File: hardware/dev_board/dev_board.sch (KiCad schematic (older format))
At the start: 3 parts

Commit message: finished schematic
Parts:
- added C? (x2): C_4u7, personal:C_0805, symbol personal:C_4u7
- added C? (x13): C_0u1, personal:C_0805, symbol personal:C_0u1
- added C?: C_220u, personal:UWT0G221MCL6GS, symbol personal:C_220u
- added C? (x2): C_8p, personal:C_0805, symbol personal:C_8p
- added C?: C_1u, personal:C_0805, symbol personal:C_1u
- added C? (x2): C_10u, personal:C_0805, symbol personal:C_10u
- added C?: C_22u, personal:C_0805, symbol personal:C_22u
- added D? (x2): D_Schottky_10V_3A, Diodes_SMD:D_SOD-323F, symbol personal:D_Schottky_10V_3A
- added D?: D_Schottky_x2_20V, personal:SOT1061, symbol personal:D_Schottky_x2_20V
- added D? (x4): LED_0805_Green, personal:LED_0805, symbol personal:LED_0805_Green
- added F? (x2): PTC_6V_1A, Resistors_SMD:R_0805_HandSoldering, symbol personal:PTC_6V_1A
- added J?: Micro_USB, Connectors_USB:USB_Micro-B_Molex_47346-0001, symbol personal:Micro_USB
- added J?: Conn_02x03, personal:TSW-103-07-F-D, symbol personal:Conn_02x03
- added J?: 105162-0001, personal:105162-0001, symbol personal:105162-0001
- added J? (x3): Conn_01x02, personal:header_01x02, symbol personal:Conn_01x02
- added J?: Conn_01x10, personal:header_01x10, symbol personal:Conn_01x10
- added J? (x3): Conn_01x04, personal:header_01x04, symbol personal:Conn_01x04
- added J?: Conn_01x06, personal:header_01x06, symbol personal:Conn_01x06
- added J?: Conn_01x11, personal:header_01x11, symbol personal:Conn_01x11
- added R?: R_1K, personal:R_0805, symbol personal:R_1K
- added R?: R_10K, personal:R_0805, symbol personal:R_10K
- added R? (x2): R_22, personal:R_0805, symbol personal:R_22
- added R?: R_120, personal:R_0805, symbol personal:R_120
- added R?: R_2K18, personal:R_0805, symbol personal:R_2K18
- added R? (x3): R_51.1, personal:R_0805, symbol personal:R_51.1
- added R? (x6): R_100K, personal:R_0805, symbol personal:R_100K
- added U?: MCP131T-300E_TT, personal:SOT-23, symbol personal:MCP131T-300E_TT
- added U?: LDO_600MA, personal:SOT-25_DIO, symbol personal:LDO_600MA
- added U?: OKL-T_1-W12P-C, personal:OKL-T1-W12P-C, symbol personal:OKL-T_1-W12P-C
- added U?: Barometer_MS5607, personal:MS561101BA03-50, symbol personal:Barometer_MS5607
- added U?: FRAM_4K, Housings_SOIC:SOIC-8_3.9x4.9mm_Pitch1.27mm, symbol personal:FRAM_4K
- added Y?: Crystal_24MHZ, personal:NX3225SA-24.000M-STD-CSR-1, symbol personal:Crystal_24MHZ
- U?: footprint drone_footprints:BMI088 -> personal:BMI088
- U?: footprint drone_footprints:LIS3MDLTR -> personal:LIS3MDLTR
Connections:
- net at U?.1 (VBAT): now also C?.1, D?.1 (K)
- net SPI2_MISO: now reaches U?.10 (PC2)
- net SPI2_MISO: now also J?.2, U?.5 (SI)
- net SPI2_MOSI: now reaches U?.11 (PC3)
- net SPI2_MOSI: now also J?.3, U?.2 (SO)
- net GND: now reaches U?.12 (VSSA)
- net GND: now also U?.12 (RES), U?.18 (VSS), U?.2 (NC), U?.2 (RES), U?.3 (GND), U?.31 (VSS), U?.4 (GNDA), U?.47 (VSS), U?.6 (GNDio), U?.63 (VSS), U?.7 (PS), C?.1, C?.1, C?.1, C?.1, C?.1, C?.1, C?.1, C?.2, C?.2, C?.2, C?.2, C?.2, C?.2, C?.2, C?.2, C?.2, C?.2, C?.2, C?.2, C?.2, C?.2, C?.2, J?.10 (GND_1), J?.11 (GND_2), J?.12 (GND_3), J?.13 (GND_4), J?.2, J?.2, J?.2, J?.4, J?.4, J?.5 (GND), J?.6, J?.6 (Pin_6), J?.6 (VSS), R?.2, R?.2, R?.2, R?.2, R?.2, R?.2, U?.11 (GND), U?.2 (GND), U?.2 (PS), U?.3 (GND), U?.3 (GND), U?.3 (VSS), U?.4 (Vss), U?.7 (GND), Y?.2, Y?.4
- net 3V3: now reaches U?.13 (VREF+)
- net 3V3: now also U?.11 (VDDIO), U?.19 (VDD), U?.3 (VDD), U?.32 (VDD), U?.48 (VDD), U?.5 (VDD), U?.6 (VDD_IO), U?.64 (VDD), C?.1, C?.1, C?.1, C?.1, C?.1, C?.1, C?.1, C?.1, C?.1, C?.1, C?.1, C?.1, C?.2, D?.2 (A), J?.1, J?.1, J?.1, J?.1 (Pin_1), J?.4 (VDD), R?.1, R?.1, R?.1, R?.1, R?.1, R?.1, R?.2, U?.2 (VDD), U?.3 (EN), U?.3 (~WP), U?.5 (VO), U?.7 (~HOLD), U?.8 (Vdd)
- net ADC_IN0: now reaches U?.14 (PA0)
- net ADC_IN0: now also J?.1
- net ADC_IN1: now reaches U?.15 (PA1)
- net ADC_IN1: now also J?.2
- net USART2_TX: now reaches U?.16 (PA2)
- net USART2_TX: now also J?.2
- net USART2_RX: now reaches U?.17 (PA3)
- net USART2_RX: now also J?.3
- net SD_DETECT: now reaches U?.2 (PC13)
- net SD_DETECT: now also J?.9 (DET), R?.2
- net PA4: now reaches U?.20 (PA4)
- net PA4: now also J?.3
- net SPI1_SCK: now reaches U?.21 (PA5)
- net SPI1_SCK: now also U?.1 (SCL/SPC), U?.8 (SCx), J?.1, U?.8 (SCLK)
- net SPI1_MISO: now reaches U?.22 (PA6)
- net SPI1_MISO: now also U?.10 (SD02), U?.15 (SD01), U?.9 (SDO/SA1), J?.2, U?.6 (SDO)
- net SPI1_MOSI: now reaches U?.23 (PA7)
- net SPI1_MOSI: now also U?.11 (SDA/SDI/SDO), U?.9 (SDx), J?.3, U?.7 (SDI/A)
- net ACCEL_CS: now reaches U?.24 (PC4)
- net ACCEL_CS: now also U?.14 (CSB1), J?.6
- net GYRO_CS: now reaches U?.25 (PC5)
- net GYRO_CS: now also U?.5 (CSB2), J?.7
- net BARO_CS: now reaches U?.26 (PB0)
- net BARO_CS: now also J?.10, U?.4 (CSB), U?.5 (CSB)
- net ~FRAM_CS: now reaches U?.27 (PB1)
- net ~FRAM_CS: now also J?.4, U?.1 (~CS)
- net SPI3_AUX_CS: now reaches U?.28 (PB2)
- net SPI3_AUX_CS: now also J?.5
- net SPI2_SCK: now reaches U?.29 (PB10)
- net SPI2_SCK: now also J?.1, U?.6 (SCK)
- net at U?.3 (PC14): now also D?.2 (A)
- net at U?.30 (VCAP1): now also C?.1
- net PB12: now reaches U?.33 (PB12)
- net PB12: now also J?.8
- net PB13: now reaches U?.34 (PB13)
- net PB13: now also J?.9
- net PB14: now reaches U?.35 (PB14)
- net PB14: now also J?.10
- net PB15: now reaches U?.36 (PB15)
- net PB15: now also J?.11
- net ACCEL_DRDY: now reaches U?.37 (PC6)
- net ACCEL_DRDY: now also U?.16 (INT1), J?.8
- net GYRO_DRDY: now reaches U?.38 (PC7)
- net GYRO_DRDY: now also U?.12 (INT3), J?.9
- net SDIO_D0: now reaches U?.39 (PC8)
- net SDIO_D0: now also J?.7 (DAT0), R?.2
- net at U?.4 (PC15): now also D?.2 (A)
- net SDIO_D1: now reaches U?.40 (PC9)
- net PA8: now reaches U?.41 (PA8)
- net PA8: now also J?.4
- net USART1_TX: now reaches U?.42 (PA9)
- net USART1_TX: now also J?.2 (Pin_2)
- net PA10: now reaches U?.43 (PA10)
- net PA10: now also J?.5
- net OTG_FS_D_N: now reaches U?.44 (PA11)
- net OTG_FS_D_N: now also R?.2
- net OTG_FS_D_P: now reaches U?.45 (PA12)
- net OTG_FS_D_P: now also R?.2
- net SWDIO: now reaches U?.46 (PA13)
- net SWDIO: now also J?.4 (Pin_4)
- net SWCLK: now reaches U?.49 (PA14)
- net SWCLK: now also J?.5 (Pin_5)
- net at U?.5 (PH0): now also C?.1, Y?.3
- net PA15: now reaches U?.50 (PA15)
- net PA15: now also J?.6
- net SDIO_D2: now reaches U?.51 (PC10)
- net SDIO_D2: now also J?.1 (DAT2), R?.2
- net SDIO_D3: now reaches U?.52 (PC11)
- net SDIO_D3: now also J?.2 (CD/DAT3), R?.2
- net SDIO_CK: now reaches U?.53 (PC12)
- net SDIO_CK: now also J?.5 (CLK)
- net SDIO_CMD: now reaches U?.54 (PD2)
- net SDIO_CMD: now also J?.3 (CMD), R?.2
- net SPI3_SCK: now reaches U?.55 (PB3)
- net SPI3_SCK: now also J?.2
- net SPI3_MISO: now reaches U?.56 (PB4)
- net SPI3_MISO: now also J?.3
- net SPI3_MOSI: now reaches U?.57 (PB5)
- net SPI3_MOSI: now also J?.4
- net I2C1_SCL: now reaches U?.58 (PB6)
- net I2C1_SCL: now also J?.2
- net USART1_RX: now reaches U?.59 (PB7)
- net USART1_RX: now also J?.3 (Pin_3)
- net at U?.6 (PH1): now also C?.2, Y?.1
- net at U?.60 (BOOT0): now also R?.1
- net PB8: now reaches U?.61 (PB8)
- net PB8: now also J?.7
- net I2C1_SDA: now reaches U?.62 (PB9)
- net I2C1_SDA: now also J?.3
- net at U?.7 (NRST): now also U?.1 (~RST)
- net MAG_CS: now reaches U?.8 (PC0)
- net MAG_CS: now also U?.10 (CS), J?.4
- net MAG_DRDY: now reaches U?.9 (PC1)
- net MAG_DRDY: now also U?.8 (DRDY), J?.5
- net at U?.4 (C1): now also C?.2
- new net: D?.2 (A), R?.1
- new net: J?.2 (D-), R?.1
- new net: J?.3 (D+), R?.1
- new net: D?.3 (K), F?.1
- new net: D?.1 (K), R?.1 (x4)
- new net: C?.2, D?.1 (K), F?.2, U?.1 (VI)
- new net: C?.2, J?.1, U?.2 (VIN)
- new net: R?.1, U?.6 (TRIM)
- new net: C?.2, U?.1 (VDD)
- new net: J?.8 (DAT1), R?.2
- new net: F?.1, J?.1
- new net 5V: D?.2 (A), D?.2 (A), F?.2, J?.1
- new net BUCK_5V: D?.1 (A), U?.4 (VOUT)
- new net USB_5V: C?.2, D?.2 (A), J?.1 (VBUS)
- no-connect marks 0 -> 5
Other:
- note added: "5V Output"
- note added: "5V Power Circuits"
- note added: "Barometer"
- note added: "Buck Converter Power\n5 < Vin <= 14"
- note added: "Debug & Programming"
- note added: "Extra Pins\n"
- note added: "I2C1 Output"
- note added: "IMU"
- note added: "LDO Power\n3.3 <= Vin < 5"
- note added: "Magnetometer"
- note added: "MicroSD"
- note added: "Non-Volatile Memory"
- note added: "Power Watchdog"
- note added: "Real Time Clock"
- note added: "SPI1 Pinout"
- note added: "SPI2 Pinout"
- note added: "SPI3 Output"
- note added: "UART2 Output"
- note added: "USB Micro"
- moved on the sheet: U?

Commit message: Fixed a few errors
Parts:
- added D8: TVS_DIODE_14V, Capacitors_SMD:C_0402, symbol personal:TVS_DIODE_14V
- added R16, R17: R_10K, personal:R_0805, symbol personal:R_10K
- gave numbers to parts that had none: 67
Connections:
- net 3V3: now also R16.1, R17.1
- net 5V: now also D8.2 (A2)
- net GND: now also D8.1 (A1)
- net I2C1_SCL: now also R16.2
- net I2C1_SDA: now also R17.2
- net SDIO_D1: now also J12.8 (DAT1), R10.2
- no-connect marks 5 -> 7
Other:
- moved on the sheet: D4, J11, J9, R5

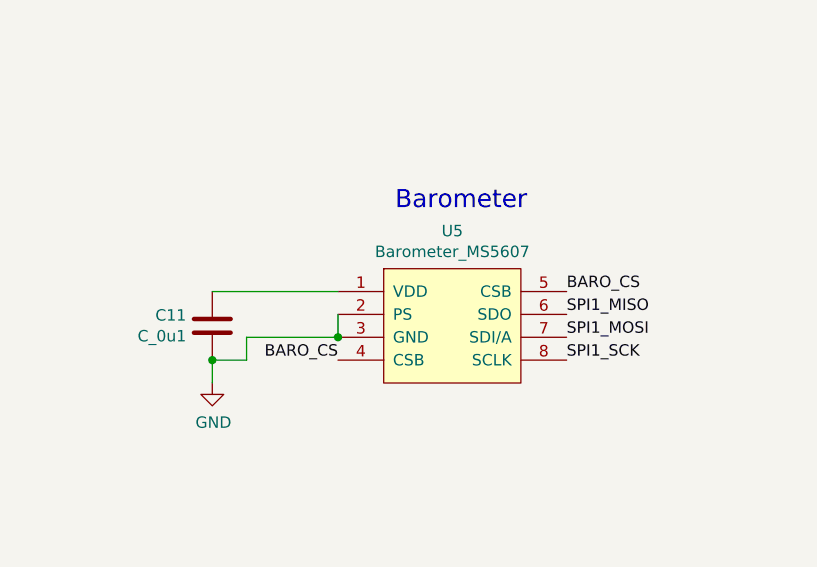
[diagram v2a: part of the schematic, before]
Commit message: fixed power issue with schematic
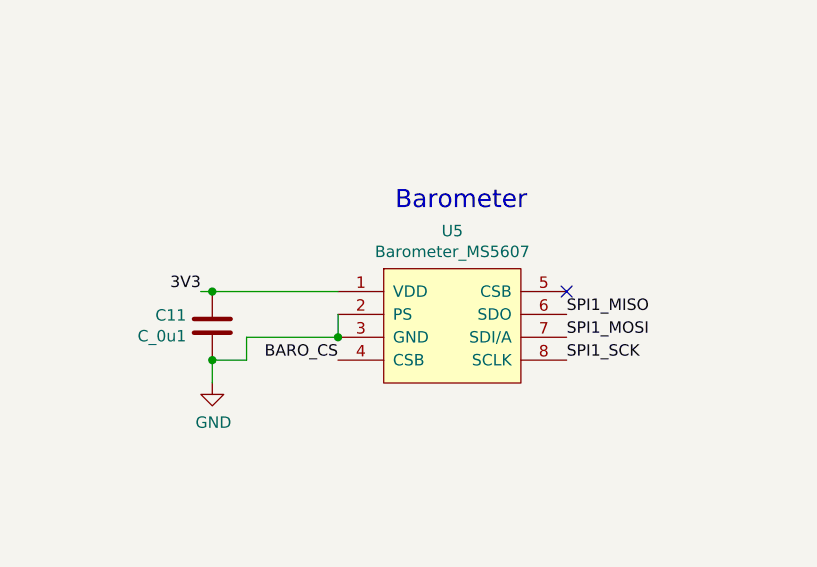
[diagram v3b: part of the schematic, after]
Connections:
- net 3V3: now also C11.2, U5.1 (VDD)
- net BARO_CS: no longer U5.5 (CSB)
- no-connect marks 7 -> 8
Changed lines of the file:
@@
 Text Label 9450 9800 2    50   ~ 0
-BARO_CS
-Text Label 10450 9500 0    50   ~ 0
 BARO_CS
 Text Label 11650 4250 2    50   ~ 0
@@
 NoConn ~ 7500 9600
 NoConn ~ 7500 9800
+Wire Wire Line
+	8900 9500 8850 9500
+Connection ~ 8900 9500
+Text Label 8850 9500 2    50   ~ 0
+3V3
+NoConn ~ 10450 9500
 $EndSCHEMATC

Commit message: added the all important axis guide and started layout
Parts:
- U7: footprint Package_QFP:LQFP-64_10x10mm_P0.5mm -> personal:STM32F401RCT6
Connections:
- net ACCEL_DRDY: now also U7.35 (PB14); no longer U7.37 (PC6)
- net BARO_CS: now also U7.33 (PB12); no longer U7.26 (PB0)
- net GYRO_DRDY: now also U7.36 (PB15); no longer U7.38 (PC7)
- net ~FRAM_CS: now also U7.34 (PB13); no longer U7.27 (PB1)
- net PB12 renamed TIM3_CH1
- net TIM3_CH1: now also U7.37 (PC6); no longer U7.33 (PB12)
- net PB13 renamed TIM3_CH2
- net TIM3_CH2: now also U7.38 (PC7); no longer U7.34 (PB13)
- net PB14 renamed TIM3_CH3
- net TIM3_CH3: now also U7.26 (PB0); no longer U7.35 (PB14)
- net PB15 renamed TIM3_CH4
- net TIM3_CH4: now also U7.27 (PB1); no longer U7.36 (PB15)
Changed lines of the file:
@@
 F 0 "U7" H 12300 5631 50  0000 C CNN
 F 1 "STM32F401RCTx" H 12300 5540 50  0000 C CNN
-F 2 "Package_QFP:LQFP-64_10x10mm_P0.5mm" H 11750 2050 50  0001 R CNN
+F 2 "personal:STM32F401RCT6" H 11750 2050 50  0001 R CNN
 F 3 "http://www.st.com/st-web-ui/static/active/en/resource/technical/document/datasheet/DM00086815.pdf" H 12350 3750 50  0001 C CNN
 	1    12350 3750
@@
 Text Label 11650 4350 2    50   ~ 0
 GYRO_CS
-Text Label 11650 4450 2    50   ~ 0
+Text Label 12950 5250 0    50   ~ 0
 ACCEL_DRDY
-Text Label 11650 4550 2    50   ~ 0
+Text Label 12950 5350 0    50   ~ 0
 GYRO_DRDY
-Text Label 12950 3950 0    50   ~ 0
+Text Label 12950 5050 0    50   ~ 0
 BARO_CS
 Text Label 11650 3850 2    50   ~ 0
@@
 Text Label 12100 7300 2    50   ~ 0
 ~FRAM_CS
-Text Label 12950 4050 0    50   ~ 0
+Text Label 12950 5150 0    50   ~ 0
 ~FRAM_CS
 $Comp
@@
 Text Label 4150 8100 0    50   ~ 0
 PB8
-Text Label 12950 5050 0    50   ~ 0
-PB12
-Text Label 12950 5150 0    50   ~ 0
-PB13
-Text Label 12950 5250 0    50   ~ 0
-PB14
-Text Label 12950 5350 0    50   ~ 0
-PB15
-Text Label 4150 8200 0    50   ~ 0
-PB12
-Text Label 4150 8300 0    50   ~ 0
-PB13
-Text Label 4150 8400 0    50   ~ 0
-PB14
-Text Label 4150 8500 0    50   ~ 0
-PB15
 Text Notes 10200 1850 0    79   ~ 0
 Power Watchdog
@@
 3V3
 NoConn ~ 10450 9500
+Text Label 12950 3950 0    50   ~ 0
+TIM3_CH3
+Text Label 12950 4050 0    50   ~ 0
+TIM3_CH4
+Text Label 4150 8400 0    50   ~ 0
+TIM3_CH3
+Text Label 4150 8500 0    50   ~ 0
+TIM3_CH4
+Text Label 11650 4450 2    50   ~ 0
+TIM3_CH1
+Text Label 11650 4550 2    50   ~ 0
+TIM3_CH2
+Text Label 4150 8200 0    50   ~ 0
+TIM3_CH1
+Text Label 4150 8300 0    50   ~ 0
+TIM3_CH2
 $EndSCHEMATC

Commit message: finished layout
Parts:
- removed U7: STM32F401RCTx, personal:STM32F401RCT6, symbol MCU_ST_STM32F4:STM32F401RCTx
- added U7: STM32F401RCTx, personal:LQFP-64_10x10mm_Pitch0.5mm, symbol personal:STM32F401RCTx
- D1, D7: footprint Diodes_SMD:D_SOD-323F -> personal:D_SOD-323F
- D8: footprint Capacitors_SMD:C_0402 -> personal:C_0402
- F1, F2: footprint Resistors_SMD:R_0805_HandSoldering -> personal:R_0805_HandSoldering
- J1: footprint Connectors_USB:USB_Micro-B_Molex_47346-0001 -> personal:USB_Micro-B_Molex_47346-0001
- U8: footprint Housings_SOIC:SOIC-8_3.9x4.9mm_Pitch1.27mm -> personal:SOIC-8_3.9x4.9mm_Pitch1.27mm
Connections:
- net PB8 is gone; now on net TIM3_CH4: J10.7
- net 3V3: now also U7.13 (VREF+), U7.19 (VDD), U7.32 (VDD), U7.48 (VDD), U7.64 (VDD)
- net ACCEL_CS: now also J5.7, U7.24 (PC4); no longer J5.6
- net ACCEL_DRDY: now also U7.35 (PB14)
- net BARO_CS: now also J5.4, U7.33 (PB12); no longer J5.10
- net GND: now also U7.12 (VSSA), U7.18 (VSS), U7.31 (VSS), U7.47 (VSS), U7.63 (VSS)
- net GYRO_CS: now also J5.6, U7.25 (PC5); no longer J5.7
- net GYRO_DRDY: now also J5.5, U7.36 (PB15); no longer J5.9
- net I2C1_SCL: now also U7.58 (PB6)
- net I2C1_SDA: now also U7.62 (PB9)
- net MAG_CS: now also J5.9, U7.15 (PA1); no longer J5.4
- net MAG_DRDY: now also J5.10, U7.14 (PA0); no longer J5.5
- net OTG_FS_D_N: now also U7.44 (PA11)
- net OTG_FS_D_P: now also U7.45 (PA12)
- net PA10: now also J10.9, U7.43 (PA10); no longer J10.5
- net PA15: now also J10.10, U7.50 (PA15); no longer J10.6
- net PA8: now also J10.8, U7.41 (PA8); no longer J10.4
- net SDIO_CK: now also U7.53 (PC12)
- net SDIO_CMD: now also U7.54 (PD2)
- net SDIO_D0: now also U7.39 (PC8)
- net SDIO_D1: now also U7.40 (PC9)
- net SDIO_D2: now also U7.51 (PC10)
- net SDIO_D3: now also U7.52 (PC11)
- net SD_DETECT: now also U7.2 (PC13)
- net SPI1_MISO: now also U7.22 (PA6)
- net SPI1_MOSI: now also U7.23 (PA7)
- net SPI1_SCK: now also U7.21 (PA5)
- net SPI2_MISO: now also U7.10 (PC2)
- net SPI2_MOSI: now also U7.11 (PC3)
- net SPI2_SCK: now also U7.29 (PB10)
- net SPI3_AUX_CS: now also U7.61 (PB8)
- net SPI3_MISO: now also U7.56 (PB4)
- net SPI3_MOSI: now also U7.57 (PB5)
- net SPI3_SCK: now also U7.55 (PB3)
- net SWCLK: now also U7.49 (PA14)
- net SWDIO: now also U7.46 (PA13)
- net TIM3_CH1: now also J10.4, U7.37 (PC6); no longer J10.8
- net TIM3_CH2: now also J10.5, U7.38 (PC7); no longer J10.9
- net TIM3_CH3: now also J10.6, U7.26 (PB0); no longer J10.10
- net TIM3_CH4: now also U7.27 (PB1); no longer J10.11
- net USART1_RX: now also U7.59 (PB7)
- net USART1_TX: now also U7.42 (PA9)
- net USART2_RX: now also U7.17 (PA3)
- net USART2_TX: now also U7.16 (PA2)
- net ~FRAM_CS: now also U7.20 (PA4)
- net at C16.1, D7.1 (K): now also U7.1 (VBAT)
- net at D5.2 (A): now also U7.3 (PC14)
- net at C15.1: now also U7.30 (VCAP1)
- net at D6.2 (A): now also U7.4 (PC15)
- net at C13.1, Y1.3: now also U7.5 (PH0)
- net at C14.2, Y1.1: now also U7.6 (PH1)
- net at R15.1: now also U7.60 (BOOT0)
- net at U6.1 (~RST): now also U7.7 (NRST)
- net ADC_IN0 renamed ADC_IN11
- net ADC_IN11: now also U7.9 (PC1)
- net ADC_IN1 renamed ADC_IN10
- net ADC_IN10: now also U7.8 (PC0)
- net PA4 renamed PB13
- net PB13: now also U7.34 (PB13)
- new net PB2: J10.11, U7.28 (PB2)
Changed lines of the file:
@@
 $EndDescr
-$Comp
-L MCU_ST_STM32F4:STM32F401RCTx U7
-U 1 1 60302E32
-P 12350 3750
-F 0 "U7" H 12300 5631 50  0000 C CNN
-F 1 "STM32F401RCTx" H 12300 5540 50  0000 C CNN
-F 2 "personal:STM32F401RCT6" H 11750 2050 50  0001 R CNN
-F 3 "http://www.st.com/st-web-ui/static/active/en/resource/technical/document/datasheet/DM00086815.pdf" H 12350 3750 50  0001 C CNN
-	1    12350 3750
-	1    0    0    -1
-$EndComp
 $Comp
 L personal:BMI088 U4
@@
 Wire Wire Line
 	12550 1550 12800 1550
-Wire Wire Line
-	12250 2050 12350 2050
-Connection ~ 12550 2050
-Connection ~ 12350 2050
-Wire Wire Line
-	12350 2050 12450 2050
-Connection ~ 12450 2050
-Wire Wire Line
-	12450 2050 12550 2050
 Wire Wire Line
 	14600 1550 14150 1550
@@
 Wire Wire Line
 	11200 3700 11200 3450
-Wire Wire Line
-	12150 5550 12250 5550
-Connection ~ 12250 5550
-Wire Wire Line
-	12250 5550 12350 5550
-Connection ~ 12350 5550
-Wire Wire Line
-	12350 5550 12450 5550
-Connection ~ 12450 5550
-Wire Wire Line
-	12450 5550 12550 5550
 $Comp
 L power:GND #PWR031
@@
 Wire Wire Line
 	12550 5600 12550 5550
-Connection ~ 12550 5550
 $Comp
 L personal:MCP131T-300E_TT U6
@@
 F 0 "J1" H 1107 1867 50  0000 C CNN
 F 1 "Micro_USB" H 1107 1776 50  0000 C CNN
-F 2 "Connectors_USB:USB_Micro-B_Molex_47346-0001" H 1650 1000 50  0001 C CNN
+F 2 "personal:USB_Micro-B_Molex_47346-0001" H 1650 1000 50  0001 C CNN
 F 3 "https://www.digikey.com/products/en?keywords=WM17141CT-ND" H 1200 1350 50  0001 C CNN
 F 4 "WM17141CT-ND" H 1600 1100 50  0001 C CNN "DPN"
@@
 F 0 "F2" H 4850 2125 50  0000 C CNN
 F 1 "PTC_6V_1A" H 4850 2034 50  0000 C CNN
-F 2 "Resistors_SMD:R_0805_HandSoldering" H 4950 2350 50  0001 L CNN
+F 2 "personal:R_0805_HandSoldering" H 4950 2350 50  0001 L CNN
 F 3 "" V 4850 1900 50  0001 C CNN
 F 4 "507-1813-1-ND" H 5250 2150 50  0001 C CNN "DPN"
@@
 F 0 "U8" H 12450 7493 50  0000 C CNN
 F 1 "FRAM_4K" H 12400 6850 50  0001 C CNN
-F 2 "Housings_SOIC:SOIC-8_3.9x4.9mm_Pitch1.27mm" H 12350 7600 50  0001 C CNN
+F 2 "personal:SOIC-8_3.9x4.9mm_Pitch1.27mm" H 12350 7600 50  0001 C CNN
 F 3 "https://www.cypress.com/file/136461/download" H 11900 7950 50  0001 C CNN
 F 4 "428-3209-ND" H 11600 7600 50  0001 C CNN "DPN"
@@
 	1    0    0    -1
 $EndComp
-Text Label 12950 2250 0    50   ~ 0
-ADC_IN0
-Text Label 12950 2350 0    50   ~ 0
-ADC_IN1
+Text Label 11650 3950 2    50   ~ 0
+ADC_IN11
+Text Label 11650 3850 2    50   ~ 0
+ADC_IN10
 Text Label 12950 2450 0    50   ~ 0
 USART2_TX
@@
 Text Label 12950 5050 0    50   ~ 0
 BARO_CS
-Text Label 11650 3850 2    50   ~ 0
+Text Label 12950 2350 0    50   ~ 0
 MAG_CS
-Text Label 11650 3950 2    50   ~ 0
+Text Label 12950 2250 0    50   ~ 0
 MAG_DRDY
 Text Label 4250 9700 0    50   ~ 0
@@
 Text Label 12100 7300 2    50   ~ 0
 ~FRAM_CS
-Text Label 12950 5150 0    50   ~ 0
+Text Label 12950 2650 0    50   ~ 0
 ~FRAM_CS
 $Comp
@@
 F 0 "F1" H 1800 4175 50  0000 C CNN
 F 1 "PTC_6V_1A" H 1800 4084 50  0000 C CNN
-F 2 "Resistors_SMD:R_0805_HandSoldering" H 1900 4400 50  0001 L CNN
+F 2 "personal:R_0805_HandSoldering" H 1900 4400 50  0001 L CNN
 F 3 "" V 1800 3950 50  0001 C CNN
 F 4 "507-1813-1-ND" H 2200 4200 50  0001 C CNN "DPN"
@@
 F 0 "D7" H 11750 1350 50  0000 C CNN
 F 1 "D_Schottky_10V_3A" H 11600 1450 50  0000 C CNN
-F 2 "Diodes_SMD:D_SOD-323F" H 12250 1850 50  0001 C CNN
+F 2 "personal:D_SOD-323F" H 12250 1850 50  0001 C CNN
 F 3 "~" H 11750 1550 50  0001 C CNN
 F 4 "1727-3852-1-ND" H 12150 1750 50  0001 C CNN "DPN"
@@
 F 0 "D1" H 2850 3600 50  0000 C CNN
 F 1 "D_Schottky_10V_3A" H 2700 3700 50  0000 C CNN
-F 2 "Diodes_SMD:D_SOD-323F" H 3350 4100 50  0001 C CNN
+F 2 "personal:D_SOD-323F" H 3350 4100 50  0001 C CNN
 F 3 "~" H 2850 3800 50  0001 C CNN
 F 4 "1727-3852-1-ND" H 3250 4000 50  0001 C CNN "DPN"
@@
 	1    0    0    -1
 $EndComp
-Text Label 12950 4150 0    50   ~ 0
+Text Label 12950 4750 0    50   ~ 0
 SPI3_AUX_CS
 $Comp
@@
 Text Label 1400 7700 0    50   ~ 0
 SPI1_MOSI
-Text Label 1400 7800 0    50   ~ 0
+Text Label 1400 8300 0    50   ~ 0
 MAG_CS
-Text Label 1400 7900 0    50   ~ 0
+Text Label 1400 8400 0    50   ~ 0
 MAG_DRDY
+Text Label 1400 8100 0    50   ~ 0
+ACCEL_CS
 Text Label 1400 8000 0    50   ~ 0
-ACCEL_CS
-Text Label 1400 8100 0    50   ~ 0
 GYRO_CS
 Text Label 1400 8200 0    50   ~ 0
 ACCEL_DRDY
-Text Label 1400 8300 0    50   ~ 0
+Text Label 1400 7900 0    50   ~ 0
 GYRO_DRDY
-Text Label 1400 8400 0    50   ~ 0
+Text Label 1400 7800 0    50   ~ 0
 BARO_CS
 Text Notes 850  7150 0    79   ~ 0
@@
 Text Label 11650 5150 2    50   ~ 0
 SD_DETECT
-Text Label 4150 7500 0    50   ~ 0
-ADC_IN0
-Text Label 4150 7600 0    50   ~ 0
-ADC_IN1
-Text Label 12950 2650 0    50   ~ 0
-PA4
-Text Label 4150 7800 0    50   ~ 0
+Text Label 4150 8200 0    50   ~ 0
 PA8
-Text Label 4150 7700 0    50   ~ 0
-PA4
 $Comp
 L personal:Conn_01x06 J4
@@
 Text Label 12950 3750 0    50   ~ 0
 PA15
-Text Label 4150 7900 0    50   ~ 0
+Text Label 4150 8300 0    50   ~ 0
 PA10
-Text Label 4150 8000 0    50   ~ 0
+Text Label 4150 8400 0    50   ~ 0
 PA15
-Text Label 12950 4750 0    50   ~ 0
-PB8
-Text Label 4150 8100 0    50   ~ 0
-PB8
+Text Label 12950 4150 0    50   ~ 0
+PB2
+Text Label 4150 8500 0    50   ~ 0
+PB2
 Text Notes 10200 1850 0    79   ~ 0
 Power Watchdog
@@
 F 0 "D8" V 5296 1971 50  0000 R CNN
 F 1 "TVS_DIODE_14V" V 5205 1971 50  0000 R CNN
-F 2 "Capacitors_SMD:C_0402" H 5250 1850 50  0001 C CNN
+F 2 "personal:C_0402" H 5250 1850 50  0001 C CNN
 F 3 "" H 5200 2050 50  0001 C CNN
 F 4 "PESD0402-140CT-ND" H 5250 2050 50  0001 C CNN "DPN"
@@
 Text Label 12950 4050 0    50   ~ 0
 TIM3_CH4
-Text Label 4150 8400 0    50   ~ 0
+Text Label 4150 8000 0    50   ~ 0
 TIM3_CH3
-Text Label 4150 8500 0    50   ~ 0
+Text Label 4150 8100 0    50   ~ 0
 TIM3_CH4
 Text Label 11650 4450 2    50   ~ 0
@@
 Text Label 11650 4550 2    50   ~ 0
 TIM3_CH2
-Text Label 4150 8200 0    50   ~ 0
+Text Label 4150 7800 0    50   ~ 0
 TIM3_CH1
-Text Label 4150 8300 0    50   ~ 0
+Text Label 4150 7900 0    50   ~ 0
 TIM3_CH2
+Text Label 12950 5150 0    50   ~ 0
+PB13
+Text Label 4150 7700 0    50   ~ 0
+PB13
+Text Label 4150 7500 0    50   ~ 0
+ADC_IN11
+Text Label 4150 7600 0    50   ~ 0
+ADC_IN10
+Wire Wire Line
+	12150 5550 12250 5550
+$Comp
+L personal:STM32F401RCTx U7
+U 1 1 6046F4F2
+P 12350 3750
+F 0 "U7" H 12300 5813 50  0000 C CNN
+F 1 "STM32F401RCTx" H 12300 5722 50  0000 C CNN
+F 2 "personal:LQFP-64_10x10mm_Pitch0.5mm" H 11750 2050 50  0001 R CNN
+F 3 "http://www.st.com/st-web-ui/static/active/en/resource/technical/document/datasheet/DM00086815.pdf" H 12350 3750 50  0001 C CNN
+F 4 "497-14047-ND" H 12300 5631 50  0000 C CNN "DPN"
+F 5 "STM32F401RCT6" H 12300 5540 50  0000 C CNN "MPN"
+	1    12350 3750
+	1    0    0    -1
+$EndComp
+Wire Wire Line
+	12450 2050 12550 2050
+Connection ~ 12550 2050
+Wire Wire Line
+	12250 5550 12350 5550
+Connection ~ 12250 5550
+Connection ~ 12550 5550
+Connection ~ 12350 5550
+Wire Wire Line
+	12350 5550 12450 5550
+Connection ~ 12450 5550
+Wire Wire Line
+	12450 5550 12550 5550
+Wire Wire Line
+	12250 2050 12350 2050
+Connection ~ 12450 2050
+Connection ~ 12350 2050
+Wire Wire Line
+	12350 2050 12450 2050
 $EndSCHEMATC
